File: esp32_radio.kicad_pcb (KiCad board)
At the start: 2 copper layers, 80 x 75 mm, 168 parts, among them J1 RP-SMA, J2 LCD_TS, J3 GS2, J4 USB_OTG, J5 Micro_SD_Card, J7 Conn_ADC, Q1 DMG3415U, Q2 Q_NPN_BCE, Q3 Q_NPN_BCE, Q4 Q_NPN_BCE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

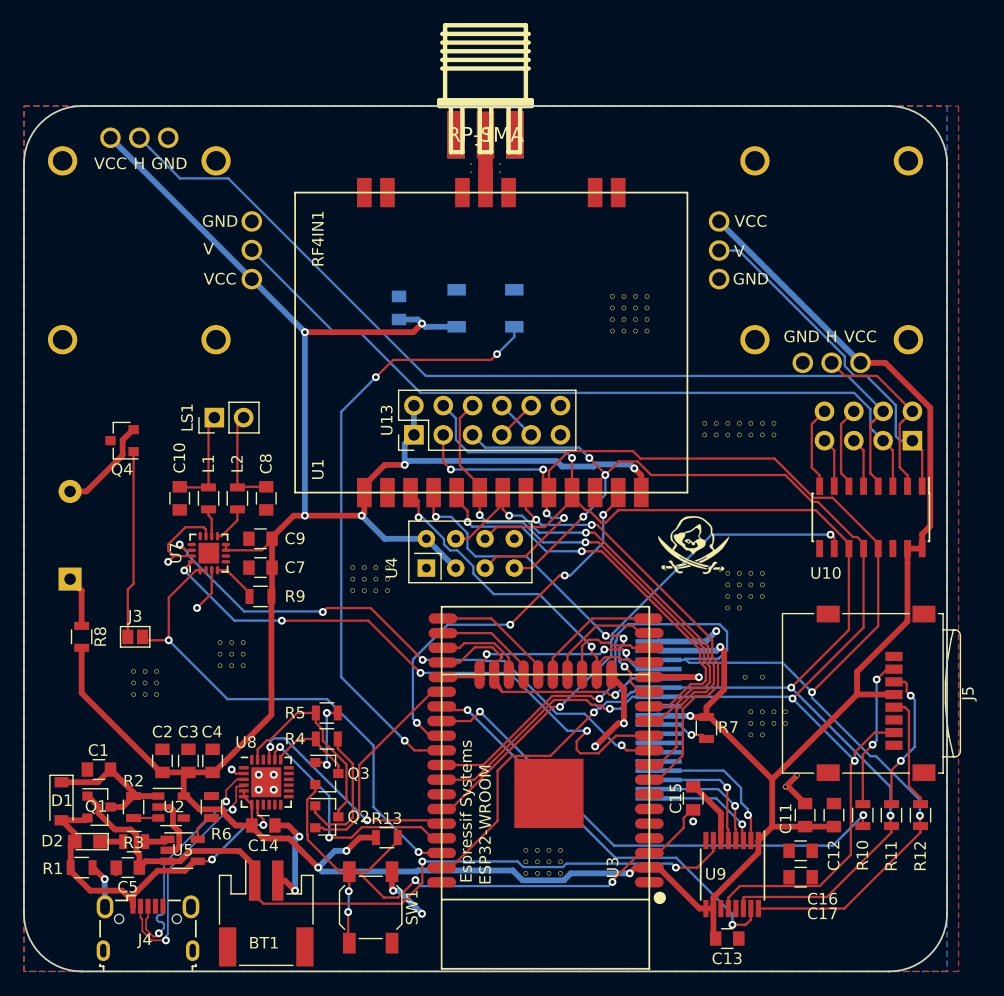
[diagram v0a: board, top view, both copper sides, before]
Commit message: drill circular
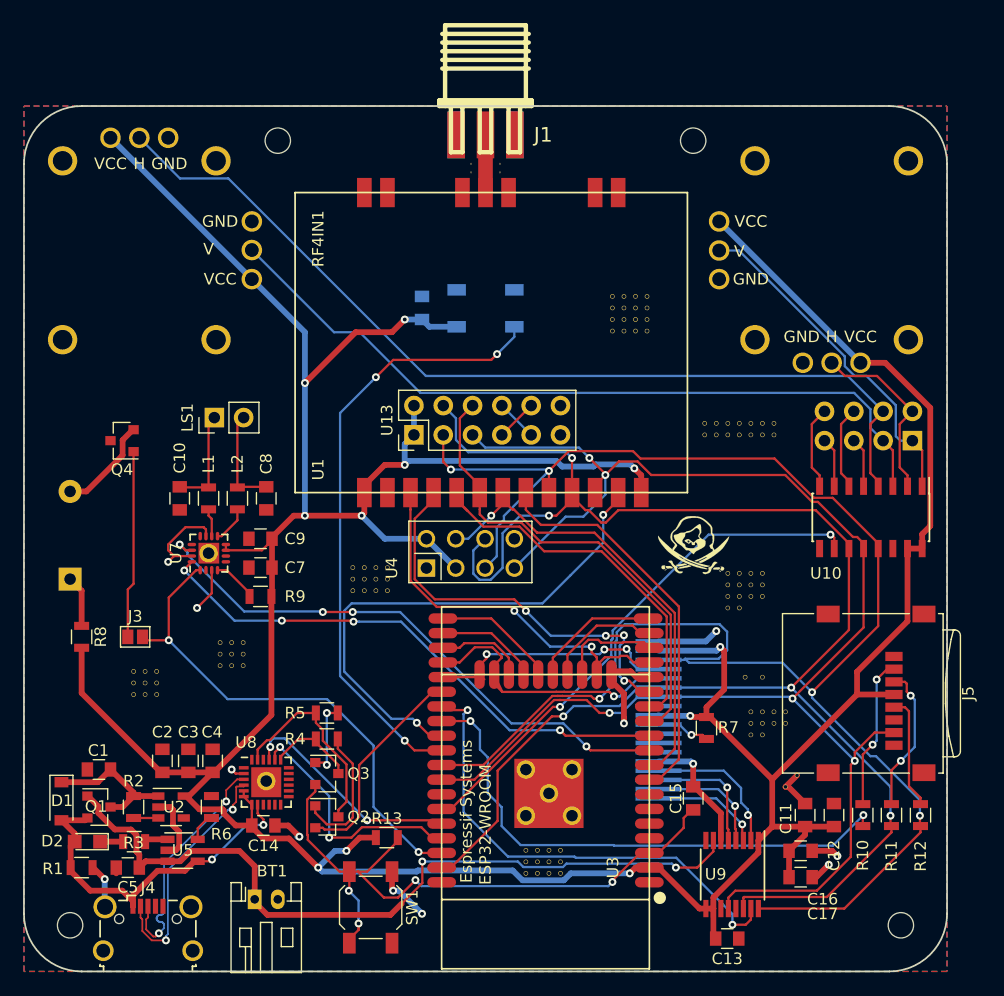
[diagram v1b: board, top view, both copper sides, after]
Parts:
- added REF**: Via, spectre:Via, F.Cu at (152.7, 98.7)
- added REF**: MountingHole_2.2mm_M2, Mounting_Holes:MountingHole_2.2mm_M2, F.Cu at (183.2, 110.1)
- added REF**: Via, spectre:Via, F.Cu at (150.7, 96.6)
- added REF**: Via, spectre:Via, F.Cu at (154.7, 100.6)
- added REF**: Via, spectre:Via, F.Cu at (150.7, 100.6)
- added REF**: Via, spectre:Via, F.Cu at (154.7, 96.6)
- added REF**: Via, spectre:Via, F.Cu at (123.2, 77.8)
- added REF**: Via, spectre:Via, F.Cu at (128.2, 97.6)
- added REF**: MountingHole_2.2mm_M2, Mounting_Holes:MountingHole_2.2mm_M2, F.Cu at (165.2, 42.1)
- added REF**: MountingHole_2.2mm_M2, Mounting_Holes:MountingHole_2.2mm_M2, F.Cu at (129.2, 42.1)
- added REF**: MountingHole_2.2mm_M2, Mounting_Holes:MountingHole_2.2mm_M2, F.Cu at (111.2, 110.1)
- BT1: footprint Connectors_JST:JST_PH_S2B-PH-SM4-TB_02x2.00mm_Angled -> Connectors_JST:JST_PH_S2B-PH-K_02x2.00mm_Angled
- J4: footprint Connectors_USB:USB_Micro-B_Wuerth-629105150521 -> Connectors_USB:USB_Micro-B_Wuerth-629105150521_CircularHoles
- moved C6 2.00 mm to (141.7, 56.6)
- moved BT1 1.60 mm to (127.2, 107.8)
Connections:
- J4 pad 2: /D+ -> /D-
- J4 pad 3: /D- -> /D+
- U7 pad 17: (no net) -> GND
- U8 pad 3: /D- -> /D+
- U8 pad 4: /D+ -> /D-
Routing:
- net /CYRF_RST: track 33.8 -> 45.8 mm, vias 4 -> 2
- net /MOSI: track 139.3 -> 147.2 mm, vias 4 -> 5
- net +3V3: track 331.1 -> 337.2 mm
- net /CS_TOUCH: track 36.3 -> 42.0 mm
- net /PE2: track 29.9 -> 35.2 mm
- net GND: track 68.5 -> 63.5 mm, vias 16 -> 12
- net /I2S_BCLK: track 50.7 -> 47.3 mm
- net /CS_CC25: track 44.7 -> 41.2 mm, vias 2 -> 0
- net /CS_CYRF: track 38.1 -> 34.8 mm, vias 2 -> 0
- net /CS_A7105: track 36.4 -> 33.3 mm, vias 2 -> 0
- net /PE1: track 31.2 -> 34.2 mm
- net /CS_SD: track 43.8 -> 46.8 mm
- net /CS_NRF24: track 44.4 -> 41.5 mm, vias 2 -> 1
- net /SCK: track 161.2 -> 159.2 mm, vias 7 -> 5
- net VBAT: track 67.3 -> 68.5 mm
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
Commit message: pull up + gerber
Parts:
- removed the REF** at (169.2, 80.6)
- removed the REF** at (168.2, 80.6)
- removed the REF** at (169.2, 79.6)
- removed the REF** at (168.2, 79.6)
- added R14: 100K, Resistors_SMD:R_0805, F.Cu at (167.1, 88.4)
- added R15: 100K, Resistors_SMD:R_0805, F.Cu at (172.0, 111.0)
- added R16: 100K, Resistors_SMD:R_0805, F.Cu at (179.8, 104.4)
- added R17: 100K, Resistors_SMD:R_0805, F.Cu at (168.7, 78.5)
- added R18: 100K, Resistors_SMD:R_0805, F.Cu at (166.6, 78.5)
- added R19: 100K, Resistors_SMD:R_0805, F.Cu at (164.3, 78.5)
- added R20: 100K, Resistors_SMD:R_0805, F.Cu at (162.1, 78.5)
- added R21: 100K, Resistors_SMD:R_0805, F.Cu at (159.8, 78.5)
- added REF**: Via, spectre:Via, F.Cu at (133.3, 112.5)
- added REF**: Via, spectre:Via, F.Cu at (128.3, 111.3)
- added REF**: Via, spectre:Via, F.Cu at (127.0, 112.5)
- added REF**: Via, spectre:Via, F.Cu at (125.7, 112.5)
- added REF**: Via, spectre:Via, F.Cu at (124.5, 112.5)
- added REF**: Via, spectre:Via, F.Cu at (127.0, 111.3)
- added REF**: Via, spectre:Via, F.Cu at (125.7, 111.3)
- added REF**: Via, spectre:Via, F.Cu at (124.5, 111.3)
- added REF**: Via, spectre:Via, F.Cu at (127.0, 110.0)
- added REF**: Via, spectre:Via, F.Cu at (125.7, 110.0)
- added REF**: Via, spectre:Via, F.Cu at (159.0, 99.1)
- added REF**: Via, spectre:Via, F.Cu at (132.1, 112.5)
- added REF**: Via, spectre:Via, F.Cu at (157.7, 99.1)
- added REF**: Via, spectre:Via, F.Cu at (159.0, 97.8)
- added REF**: Via, spectre:Via, F.Cu at (157.7, 97.8)
- added REF**: Via, spectre:Via, F.Cu at (159.0, 96.5)
- added REF**: Via, spectre:Via, F.Cu at (157.7, 96.5)
- added REF**: Via, spectre:Via, F.Cu at (159.0, 101.6)
- added REF**: Via, spectre:Via, F.Cu at (157.7, 101.6)
- added REF**: Via, spectre:Via, F.Cu at (185.9, 87.6)
- added REF**: Via, spectre:Via, F.Cu at (184.7, 87.6)
- added REF**: Via, spectre:Via, F.Cu at (124.5, 110.0)
- added REF**: Via, spectre:Via, F.Cu at (130.8, 112.5)
- added REF**: Via, spectre:Via, F.Cu at (159.0, 100.3)
- added REF**: Via, spectre:Via, F.Cu at (157.7, 100.3)
- added REF**: Via, spectre:Via, F.Cu at (185.9, 86.4)
- added REF**: Via, spectre:Via, F.Cu at (184.7, 86.4)
- added REF**: Via, spectre:Via, F.Cu at (129.5, 112.5)
- added REF**: Via, spectre:Via, F.Cu at (128.3, 112.5)
- added REF**: Via, spectre:Via, F.Cu at (133.3, 111.3)
- added REF**: Via, spectre:Via, F.Cu at (132.1, 111.3)
- added REF**: Via, spectre:Via, F.Cu at (130.8, 111.3)
- added REF**: Via, spectre:Via, F.Cu at (129.5, 111.3)
- C13: value 100nF -> 0.1uF
- R7: value 3.9R -> 3.9
- R8: value 4.7R -> 4.7
- moved G*** 6.66 mm to (171.7, 75.7)
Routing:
- net +3V3: track 337.2 -> 362.6 mm, vias 11 -> 13
- net GND: track 63.5 -> 71.7 mm, vias 12 -> 13
- net /CS_ADC: track 46.1 -> 52.5 mm, vias 2 -> 3
- net /CS_CYRF: track 34.8 -> 40.8 mm
- net /CS_A7105: track 33.3 -> 38.1 mm, vias 0 -> 2
- net /MISO: track 137.2 -> 141.5 mm
- net /CS_LCD: track 25.6 -> 29.7 mm, vias 1 -> 2
- net /CS_NRF24: track 41.5 -> 45.0 mm
- net /CS_CC25: track 41.2 -> 43.2 mm
- net /CS_SD: track 46.8 -> 48.8 mm
- net /CS_TOUCH: track 42.0 -> 43.8 mm
- net /MOSI: track 147.2 -> 148.9 mm

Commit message: test 3d + 5.0
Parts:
- removed the REF** at (133.3, 112.5)
- removed the REF** at (128.3, 111.3)
- removed the REF** at (166.2, 67.6)
- removed the REF** at (173.2, 91.6)
- removed the REF** at (172.2, 91.6)
- removed the REF** at (171.2, 91.6)
- removed the REF** at (170.2, 91.6)
- removed the REF** at (153.7, 103.6)
- removed the REF** at (152.7, 103.6)
- removed the REF** at (151.7, 103.6)
- removed the REF** at (150.7, 103.6)
- removed the REF** at (138.7, 81.1)
- removed the REF** at (127.0, 112.5)
- removed the REF** at (137.7, 81.1)
- removed the REF** at (136.7, 81.1)
- removed the REF** at (135.7, 81.1)
- removed the REF** at (118.7, 90.1)
- removed the REF** at (117.7, 90.1)
- removed the REF** at (116.7, 90.1)
- removed the REF** at (126.2, 87.6)
- removed the REF** at (125.2, 87.6)
- removed the REF** at (124.2, 87.6)
- removed the REF** at (138.7, 80.1)
- removed the REF** at (125.7, 112.5)
- removed the REF** at (137.7, 80.1)
- removed the REF** at (136.7, 80.1)
- removed the REF** at (135.7, 80.1)
- removed the REF** at (118.7, 89.1)
- removed the REF** at (117.7, 89.1)
- removed the REF** at (116.7, 89.1)
- removed the REF** at (126.2, 86.6)
- removed the REF** at (125.2, 86.6)
- removed the REF** at (124.2, 86.6)
- removed the REF** at (138.7, 79.1)
- removed the REF** at (124.5, 112.5)
- removed the REF** at (137.7, 79.1)
- removed the REF** at (136.7, 79.1)
- removed the REF** at (135.7, 79.1)
- removed the REF** at (118.7, 88.1)
- removed the REF** at (117.7, 88.1)
- removed the REF** at (116.7, 88.1)
- removed the REF** at (126.2, 85.6)
- removed the REF** at (125.2, 85.6)
- removed the REF** at (127.0, 111.3)
- removed the REF** at (124.2, 85.6)
- removed the REF** at (125.7, 111.3)
- removed the REF** at (124.5, 111.3)
- removed the REF** at (127.0, 110.0)
- removed the REF** at (125.7, 110.0)
- removed the REF** at (159.0, 99.1)
- removed the REF** at (132.1, 112.5)
- removed the REF** at (157.7, 99.1)
- removed the REF** at (159.0, 97.8)
- removed the REF** at (157.7, 97.8)
- removed the REF** at (159.0, 96.5)
- removed the REF** at (157.7, 96.5)
- removed the REF** at (159.0, 101.6)
- removed the REF** at (157.7, 101.6)
- removed the REF** at (185.9, 87.6)
- removed the REF** at (184.7, 87.6)
- removed the REF** at (124.5, 110.0)
- removed the REF** at (130.8, 112.5)
- removed the REF** at (159.0, 100.3)
- removed the REF** at (157.7, 100.3)
- removed the REF** at (185.9, 86.4)
- removed the REF** at (184.7, 86.4)
- removed the REF** at (129.5, 112.5)
- removed the REF** at (172.2, 66.6)
- removed the REF** at (172.2, 67.6)
- removed the REF** at (161.2, 58.6)
- removed the REF** at (160.2, 58.6)
- removed the REF** at (159.2, 58.6)
- removed the REF** at (158.2, 58.6)
- removed the REF** at (171.2, 88.6)
- removed the REF** at (128.3, 112.5)
- removed the REF** at (169.7, 88.6)
- removed the REF** at (169.2, 82.6)
- removed the REF** at (168.2, 82.6)
- removed the REF** at (171.2, 66.6)
- removed the REF** at (171.2, 67.6)
- removed the REF** at (161.2, 57.6)
- removed the REF** at (160.2, 57.6)
- removed the REF** at (159.2, 57.6)
- removed the REF** at (158.2, 57.6)
- removed the REF** at (171.2, 81.6)
- removed the REF** at (133.3, 111.3)
- removed the REF** at (170.2, 81.6)
- removed the REF** at (169.2, 81.6)
- removed the REF** at (168.2, 81.6)
- removed the REF** at (170.2, 66.6)
- removed the REF** at (170.2, 67.6)
- removed the REF** at (161.2, 56.6)
- removed the REF** at (160.2, 56.6)
- removed the REF** at (159.2, 56.6)
- removed the REF** at (158.2, 56.6)
- removed the REF** at (171.2, 80.6)
- removed the REF** at (132.1, 111.3)
- removed the REF** at (170.2, 80.6)
- removed the REF** at (169.2, 66.6)
- removed the REF** at (169.2, 67.6)
- removed the REF** at (161.2, 55.6)
- removed the REF** at (160.2, 55.6)
- removed the REF** at (159.2, 55.6)
- removed the REF** at (158.2, 55.6)
- removed the REF** at (171.2, 79.6)
- removed the REF** at (170.2, 79.6)
- removed the REF** at (168.2, 66.6)
- removed the REF** at (130.8, 111.3)
- removed the REF** at (168.2, 67.6)
- removed the REF** at (174.2, 97.1)
- removed the REF** at (173.2, 98.1)
- removed the REF** at (171.2, 93.6)
- removed the REF** at (170.2, 93.6)
- removed the REF** at (153.7, 105.6)
- removed the REF** at (152.7, 105.6)
- removed the REF** at (151.7, 105.6)
- removed the REF** at (150.7, 105.6)
- removed the REF** at (167.2, 66.6)
- removed the REF** at (129.5, 111.3)
- removed the REF** at (167.2, 67.6)
- removed the REF** at (173.2, 92.6)
- removed the REF** at (172.2, 92.6)
- removed the REF** at (171.2, 92.6)
- removed the REF** at (170.2, 92.6)
- removed the REF** at (153.7, 104.6)
- removed the REF** at (152.7, 104.6)
- removed the REF** at (151.7, 104.6)
- removed the REF** at (150.7, 104.6)
- removed the REF** at (166.2, 66.6)
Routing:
- net GND: track 71.7 -> 67.7 mm, vias 13 -> 127

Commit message: drc
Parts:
- removed G*** (x2): LOGO, spectre:bitmap
- removed G***: LOGO, spectre:Logo
- removed J3: GS2, Connectors:GS2
- removed REF** (x11): Via, spectre:Via
- removed REF** (x4): MountingHole_2.2mm_M2, Mounting_Holes:MountingHole_2.2mm_M2
- added JP1: SolderJumper_3_Bridged12, Jumper:SolderJumper-3_P1.3mm_Bridged12_RoundedPad1.0x1.5mm, F.Cu at (139.2, 97.3)
- added MH1: MountingHole, Mounting_Holes:MountingHole_2.2mm_M2_Pad, F.Cu at (130.2, 43.1)
- added MH2: MountingHole, Mounting_Holes:MountingHole_2.2mm_M2_Pad, F.Cu at (164.2, 43.1)
- added MH3: MountingHole, Mounting_Holes:MountingHole_2.2mm_M2_Pad, F.Cu at (110.2, 110.1)
- added MH4: MountingHole, Mounting_Holes:MountingHole_2.2mm_M2_Pad, F.Cu at (184.2, 110.1)
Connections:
- Q4 pad 1: Net-(J3-Pad1) -> /I2S_DATA
- U11 pad 5: +3V3 -> /INT_ADC_CH0
- U11 pad 6: /EXT_ADC_CH1 -> GND
- U12 pad 5: +3V3 -> /INT_ADC_CH2
- U12 pad 6: /EXT_ADC_CH3 -> GND
- U3 pad 36: /I2S_DATA -> /IN+I2S_D
- U9 pad 11: Net-(U9-Pad11) -> /TS_IRQ
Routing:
- net /INT_ADC_CH3: track 0.00 -> 83.7 mm, vias 0 -> 3
- net /EXT_ADC_CH3: track 81.5 -> 7.23 mm
- net /INT_ADC_CH2: track 0.00 -> 71.7 mm, vias 0 -> 3
- net /EXT_ADC_CH2: track 66.8 -> 4.30 mm
- net /INT_ADC_CH0: track 0.00 -> 58.9 mm, vias 0 -> 1
- net /INT_ADC_CH1: track 0.00 -> 48.1 mm, vias 0 -> 3
- net /TS_IRQ: track 0.00 -> 36.8 mm, vias 0 -> 4
- net /EXT_ADC_CH0: track 29.9 -> 4.30 mm
- net /I2S_DATA: track 44.2 -> 63.6 mm
- net Net-(J3-Pad1): track 16.3 -> 0.00 mm
- net GND: track 67.7 -> 81.3 mm, vias 127 -> 136
- net /IN+I2S_D: track 0.00 -> 9.87 mm, vias 0 -> 2
- net /EXT_ADC_CH1: track 16.0 -> 7.23 mm
- net /CYRF_RST: track 45.8 -> 43.3 mm
- net /CS_TOUCH: track 43.8 -> 45.7 mm
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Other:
- board text added: "Spectre-Tx Multiprocol Transmitter Proto V5"
- board text removed: "Spectre-Tx Multiprocol Transmitter Proto V4"
